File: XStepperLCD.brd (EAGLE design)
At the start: 49.5 x 48.3 mm, 27 parts, among them Q2 16 MHZ, U1 LCD-16X2NOHOLES

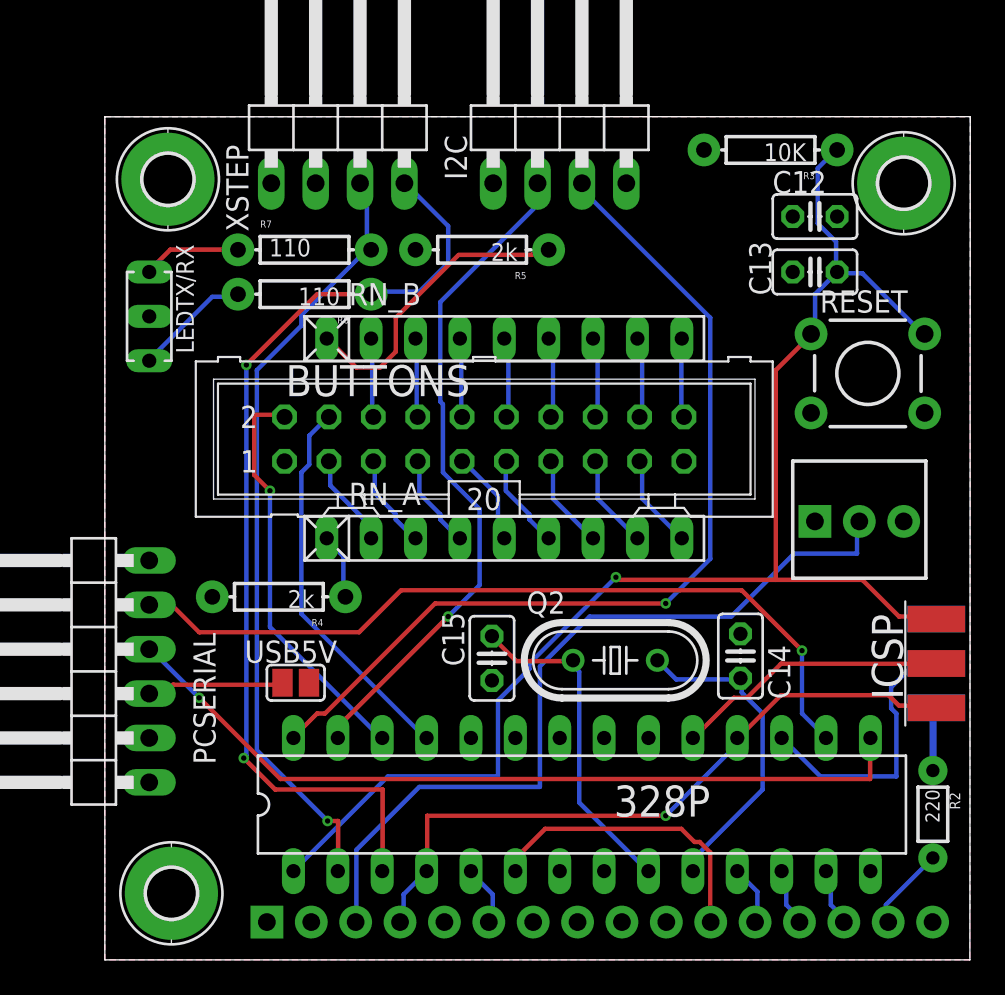
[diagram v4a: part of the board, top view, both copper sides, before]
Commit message: - published to ITEAD order number 100015612
- official Version XLCD 0.1
- add some text
- 3 pin header
- changes from Matt
- GND Polygon fix
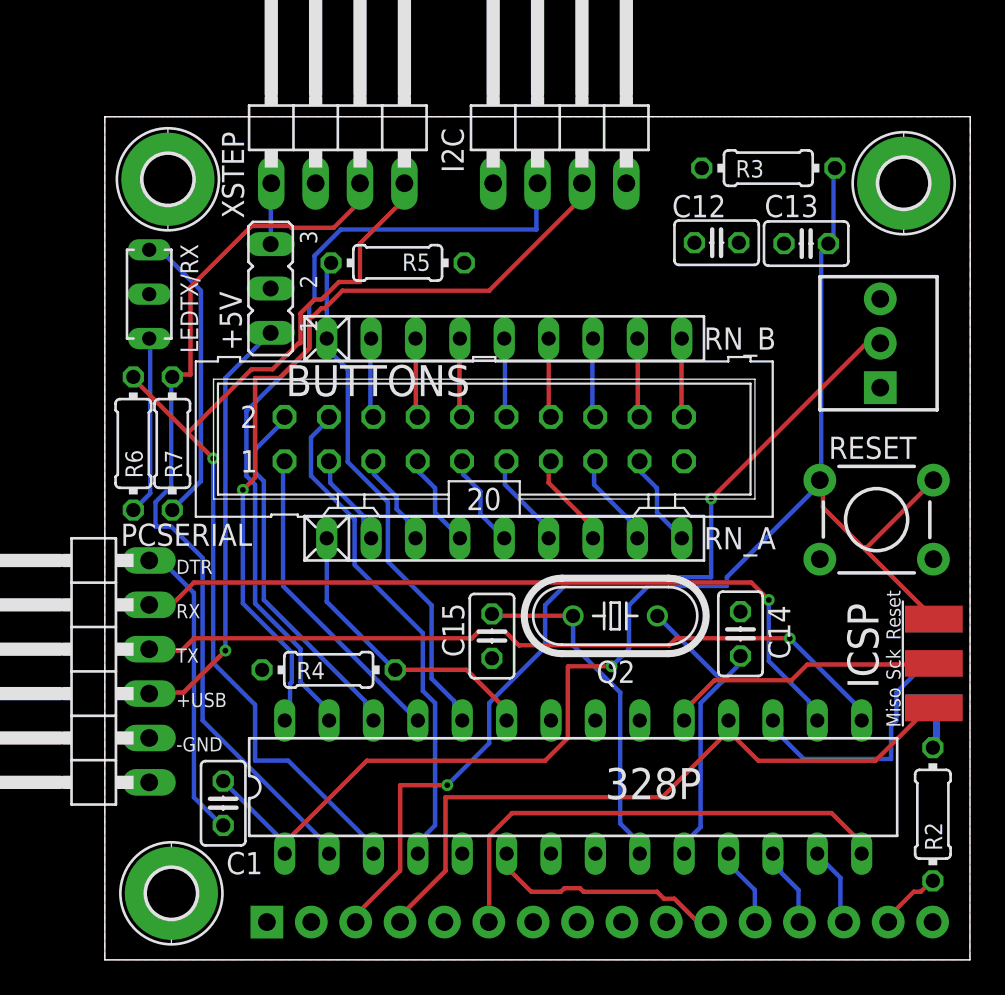
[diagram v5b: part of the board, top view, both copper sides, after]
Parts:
- removed USB5V: (no value), jumper:SJ
- added +5V: (no value), jumper:JP2
- added C1: 0.1uF, resistor:C025-025X050
- R2: device SparkFun-Resistors:1/6W-RES -> resistor:0204/7
- R3, R4, R5, R6, R7: device SparkFun-Resistors:AXIAL-0.3 -> resistor:0204/7
- moved R7 13.4 mm to (3.86, 29.6), turned to 90 degrees
- moved R6 13.0 mm to (1.63, 29.6), turned to 270 degrees
- moved R1 9.93 mm to (44.1, 35.3), turned to 90 degrees
- moved RESET 8.38 mm to (44.2, 25.2)
- moved C12 5.82 mm to (35.0, 41.0)
- moved R4 5.06 mm to (12.8, 16.6)
- moved R5 4.89 mm to (16.8, 39.9), turned to 0 degrees
- moved Q2 2.54 mm to (29.2, 19.7)
- moved C13 1.70 mm to (40.1, 41.0)
- moved LEDTX/RX 1.27 mm to (2.54, 38.1)
- moved C14 1.27 mm to (36.4, 18.7)
- moved C15 1.27 mm to (22.2, 18.5)
- moved 328P 1.12 mm to (26.8, 9.89)
- moved R3 1.05 mm to (38.0, 45.3)
- moved ICSP 0.14 mm to (47.5, 17.0)
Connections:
- removed net E: 328P.5, U1.6
- removed net N$3: R4.P$1, RN_A.1
- new net ENABLE: 328P.14, U1.6
- new net POT_SELECT: 328P.25, BUTTONS.1
- new net XSTEP_5V: +5V.3, XSTEP.1
- net BUTTONS_A: now also R4.1, RN_A.1
- net BUTTONS_B: now also R5.1, RN_B.1
- net GND: no longer BUTTONS.1, U1.10, U1.7, U1.8, U1.9
- net N$14: now also C1.1, PCSERIAL.6; no longer R5.P$1, RN_B.1
- net N$21: now also R6.2; no longer R6.P$2
- net N$22: now also R7.1; no longer R7.P$1
- net POT_A: now also 328P.4; no longer 328P.25
- net RESET: now also C1.2, R3.1; no longer R3.P$1
- net RS/MISO: no longer 328P.4
- net RX: now also R6.1; no longer R6.P$1
- net TX: now also R7.2; no longer R7.P$2
- net USB_5V: now also +5V.1; no longer USB5V.1
- net VCC: now also +5V.2, R3.2, R4.2, R5.2; no longer R3.P$2, R4.P$2, R5.P$2, USB5V.2, XSTEP.1
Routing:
- net BUTTONS_B: track 0.00 -> 29.5 mm
- net ENABLE: track 0.00 -> 28.3 mm
- net POT_SELECT: track 0.00 -> 18.1 mm
- net BUTTONS_A: track 0.00 -> 17.3 mm
- net USB_5V: track 7.90 -> 24.6 mm, vias 0 -> 1
- net N$22: track 5.65 -> 17.2 mm
- net SDA: track 38.6 -> 46.2 mm, vias 1 -> 0
- net POT_A: track 22.0 -> 28.8 mm
- net SCL: track 52.7 -> 46.1 mm
- net N$1: track 45.8 -> 52.4 mm, vias 0 -> 2
- net TX: track 45.1 -> 51.5 mm, vias 1 -> 0
- net N$3: track 3.80 -> 0.00 mm
- net RESET: track 81.0 -> 84.6 mm
- net E: track 3.51 -> 0.00 mm
- net XSTEP_5V: track 0.00 -> 3.49 mm
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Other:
- board text added: "+USB"
- board text added: "-GND"
- board text added: "DTR"
- board text added: "Miso"
- board text added: "RX"
- board text added: "Reset"
- board text added: "Sck"
- board text added: "TX"
- board text added: "XSTEP 0.1 / 082013"

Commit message: - rename all mySerial to grblSerial
- add and use phi_interfaces for rotary encoder
- change intervall to 500ms and 1000ms for threads
- send reset if connected to grbl for UniversalGcodeSender
- add call_button
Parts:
- RN_A, RN_B: value 330 -> 680
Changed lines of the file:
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@@
 <attribute name="VALUE" x="21.715" y="34.885" size="1.778" layer="27" ratio="10"/>
 </element>
-<element name="RN_A" library="resistor-net" package="RN-9" value="330" x="22.86" y="24.13" smashed="yes">
+<element name="RN_A" library="resistor-net" package="RN-9" value="680" x="22.86" y="24.13" smashed="yes">
 <attribute name="OC_NEWARK" value="unknown" x="22.86" y="24.13" size="1.778" layer="27" display="off"/>
 <attribute name="MPN" value="" x="22.86" y="24.13" size="1.778" layer="27" display="off"/>
@@
 <attribute name="VALUE" x="14.4356" y="17.0826" size="0.9906" layer="27" ratio="10" rot="R180"/>
 </element>
-<element name="RN_B" library="resistor-net" package="RN-9" value="330" x="22.86" y="35.56" smashed="yes">
+<element name="RN_B" library="resistor-net" package="RN-9" value="680" x="22.86" y="35.56" smashed="yes">
 <attribute name="OC_NEWARK" value="unknown" x="22.86" y="35.56" size="1.778" layer="27" display="off"/>
 <attribute name="MPN" value="" x="22.86" y="35.56" size="1.778" layer="27" display="off"/>
@@
 </signal>
 </signals>
-<errors>
-</errors>
 </board>
 </drawing>

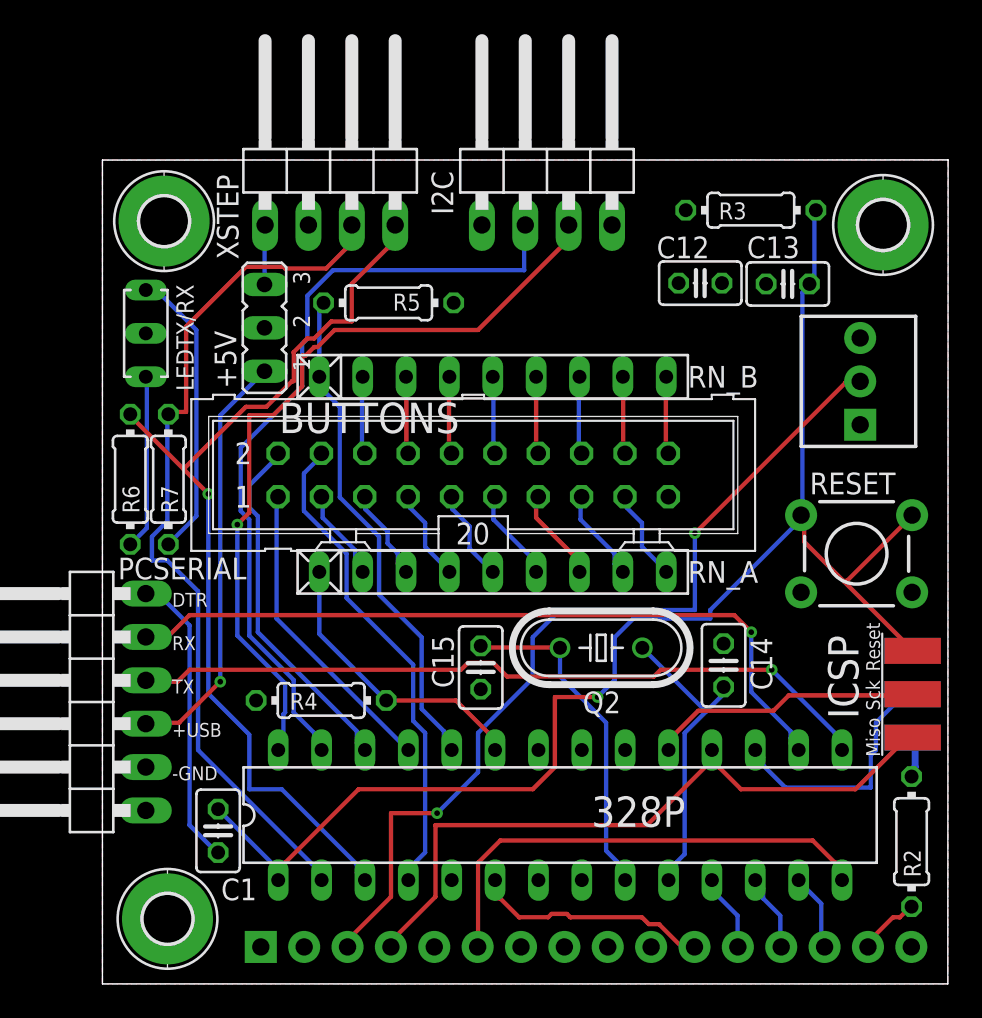
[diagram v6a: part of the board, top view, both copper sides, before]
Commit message: - change to 0.2 and produce pcb
- change all resistors and caps to SMD 1206
- change RX/TX Wires to USB_RXD/USB_TXD
- move RX/TX to Pin 14 and pin 15
- use Pin 4,5 for RotaryEncoder
- use POT_Select on Pin 16
- move Enable to mosi pin
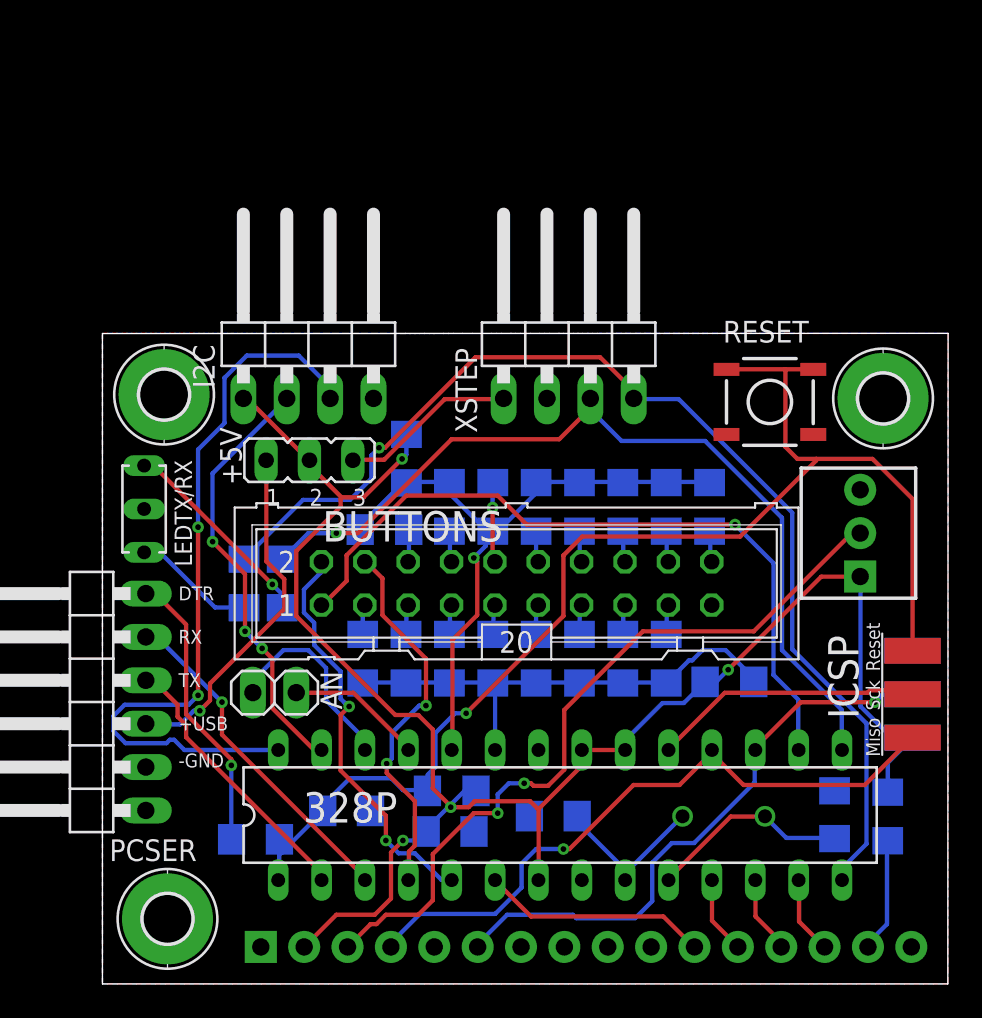
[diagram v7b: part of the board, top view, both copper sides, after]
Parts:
- removed RN_A, RN_B: 680, resistor-net:RN-9
- added AN: Analog, pinhead:1X02
- added R10, R11, R12, R13, R14, R15, R16, R17, R18, R19, R20, R21, R22, R23, R8, R9: 680, resistor:R1206
- +5V: value (none) -> USB_VCC
- C1, C12, C13, C14, C15: device resistor:C025-025X050 -> resistor:C1206
- R2, R3, R4, R5, R6, R7: device resistor:0204/7 -> resistor:R1206
- RESET: device SparkFun:TACTILE-PTH -> SparkFun:TACTILE_SWITCH_SMD
- moved C13 40.3 mm to (14.3, 10.1), flipped to the bottom
- moved R3 38.3 mm to (20.5, 11.3), flipped to the bottom
- moved C12 35.3 mm to (20.4, 8.93), flipped to the bottom, turned to 0 degrees
- moved R4 23.9 mm to (36.7, 17.7), flipped to the bottom, turned to 0 degrees
- moved I2C 17.3 mm to (12.1, 38.1)
- moved XSTEP 17.3 mm to (27.3, 38.1)
- moved Q2 12.2 mm to (36.4, 9.81), flipped to the bottom, turned to 180 degrees
- moved C14 10.9 mm to (42.9, 9.91), flipped to the bottom
- moved LEDTX/RX 10.3 mm to (2.44, 27.8)
- moved RESET 10.2 mm to (39.1, 34.1)
- moved H6 10.2 mm to (45.7, 34.3)
- moved H5 10.2 mm to (3.61, 34.5)
- moved C15 9.69 mm to (26.4, 9.82), flipped to the bottom, turned to 0 degrees
- moved R5 9.18 mm to (17.8, 30.8), flipped to the bottom, turned to 90 degrees
- moved R6 9.04 mm to (8.29, 23.5), flipped to the bottom
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- renumbered PCSERIAL to PCSER
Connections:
- removed net ENABLE: 328P.14, U1.6
- removed net MOSI: 328P.17, ICSP.MOSI
- new net BUTTONS_C: 328P.25, AN.1
- new net BUTTONS_D: 328P.26, AN.2
- new net ENABLE/MOSI: 328P.17, ICSP.MOSI, U1.6
- net BUTTONS_A: now also R16.2, R17.2, R18.2, R19.2, R20.2, R21.2, R22.2, R23.2; no longer RN_A.1
- net BUTTONS_B: now also R10.2, R11.2, R12.2, R13.2, R14.2, R15.2, R8.2, R9.2; no longer RN_B.1
- net N$10: now also R22.1; no longer RN_A.3
- net N$11: now also R10.1; no longer RN_B.4
- net N$12: now also R11.1; no longer RN_B.5
- net N$13: now also R12.1; no longer RN_B.6
- net N$15: now also R13.1; no longer RN_B.7
- net N$16: now also R21.1; no longer RN_A.4
- net N$17: now also R20.1; no longer RN_A.5
- net N$18: now also R19.1; no longer RN_A.6
- net N$19: now also R14.1; no longer RN_B.8
- net N$20: now also R15.1; no longer RN_B.9
- net N$4: now also R18.1; no longer RN_A.7
- net N$5: now also R17.1; no longer RN_A.8
- net N$6: now also R16.1; no longer RN_A.9
- net N$7: now also R8.1; no longer RN_B.2
- net N$8: now also R9.1; no longer RN_B.3
- net N$9: now also R23.1; no longer RN_A.2
- net POT_B: now also 328P.5; no longer 328P.26
- net POT_SELECT: now also 328P.16; no longer 328P.25
- net RX: now also 328P.14; no longer 328P.3
- net TX: now also 328P.15; no longer 328P.2
- net USB_RXD: now also 328P.3; no longer 328P.16
- net USB_TXD: now also 328P.2; no longer 328P.15
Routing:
- net VCC: track 2.44 -> 104.4 mm, vias 0 -> 4
- net ENABLE/MOSI: track 0.00 -> 34.4 mm, vias 0 -> 1
- net ENABLE: track 28.3 -> 0.00 mm
- net USB_TXD: track 44.1 -> 16.2 mm, vias 1 -> 0
- net POT_SELECT: track 18.1 -> 43.3 mm, vias 0 -> 1
- net USB_RXD: track 44.5 -> 19.9 mm
- net SDA: track 46.2 -> 25.3 mm, vias 0 -> 3
- net MOSI: track 14.7 -> 0.00 mm
- net BUTTONS_D: track 0.00 -> 11.9 mm
- net BUTTONS_A: track 17.3 -> 28.7 mm
- net BUTTONS_B: track 29.5 -> 40.0 mm, vias 0 -> 1
- net RX: track 55.5 -> 65.8 mm
- net N$33: track 19.9 -> 10.0 mm
- net RESET: track 84.6 -> 76.1 mm
- net BUTTONS_C: track 0.00 -> 8.05 mm
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- added copper zone on layer 1, net GND
- removed copper zone on layer 1, net VCC
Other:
- board size 49.5 x 48.3 mm -> 49.5 x 38.1 mm
- board text added: "XSTEP 0.2 / 092013"
- board text removed: "XSTEP 0.1 / 082013"
